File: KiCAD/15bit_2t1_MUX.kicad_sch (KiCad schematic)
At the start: 4 parts, among them U48 74HC257, U49 74HC257, U50 74HC257, U51 74HC257

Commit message: finished schematics and footprint assignments; need to figure out +5v connection issue
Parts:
- U48, U49, U50, U51: footprint (none) -> Package_DIP:DIP-16_W7.62mm
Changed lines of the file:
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@@
 			)
 		)
-		(property "Footprint" ""
+		(property "Footprint" "Package_DIP:DIP-16_W7.62mm"
 			(at 203.2 64.77 0)
 			(effects
@@
 			)
 		)
-		(property "Footprint" ""
+		(property "Footprint" "Package_DIP:DIP-16_W7.62mm"
 			(at 119.38 64.77 0)
 			(effects
@@
 			)
 		)
-		(property "Footprint" ""
+		(property "Footprint" "Package_DIP:DIP-16_W7.62mm"
 			(at 78.74 64.77 0)
 			(effects
@@
 			)
 		)
-		(property "Footprint" ""
+		(property "Footprint" "Package_DIP:DIP-16_W7.62mm"
 			(at 161.29 64.77 0)
 			(effects

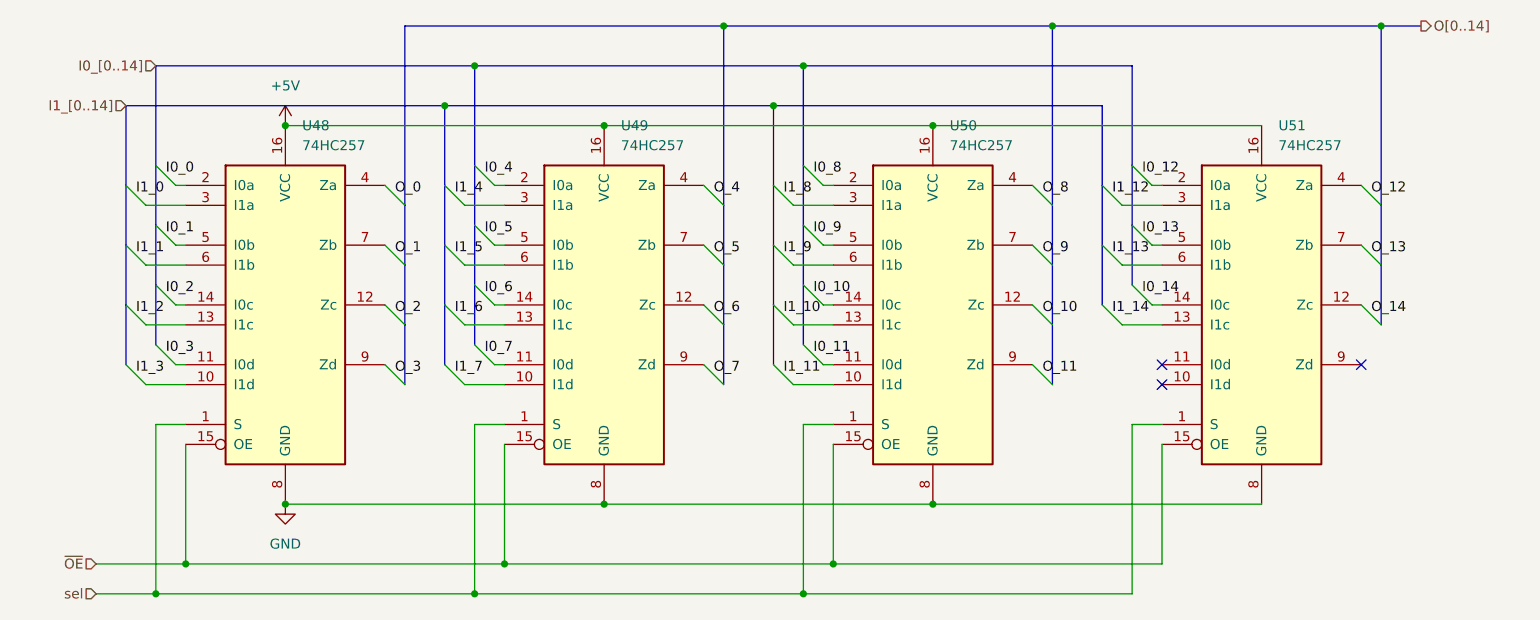
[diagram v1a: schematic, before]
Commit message: fix multiple ERCs that made RAM addrs not connecting
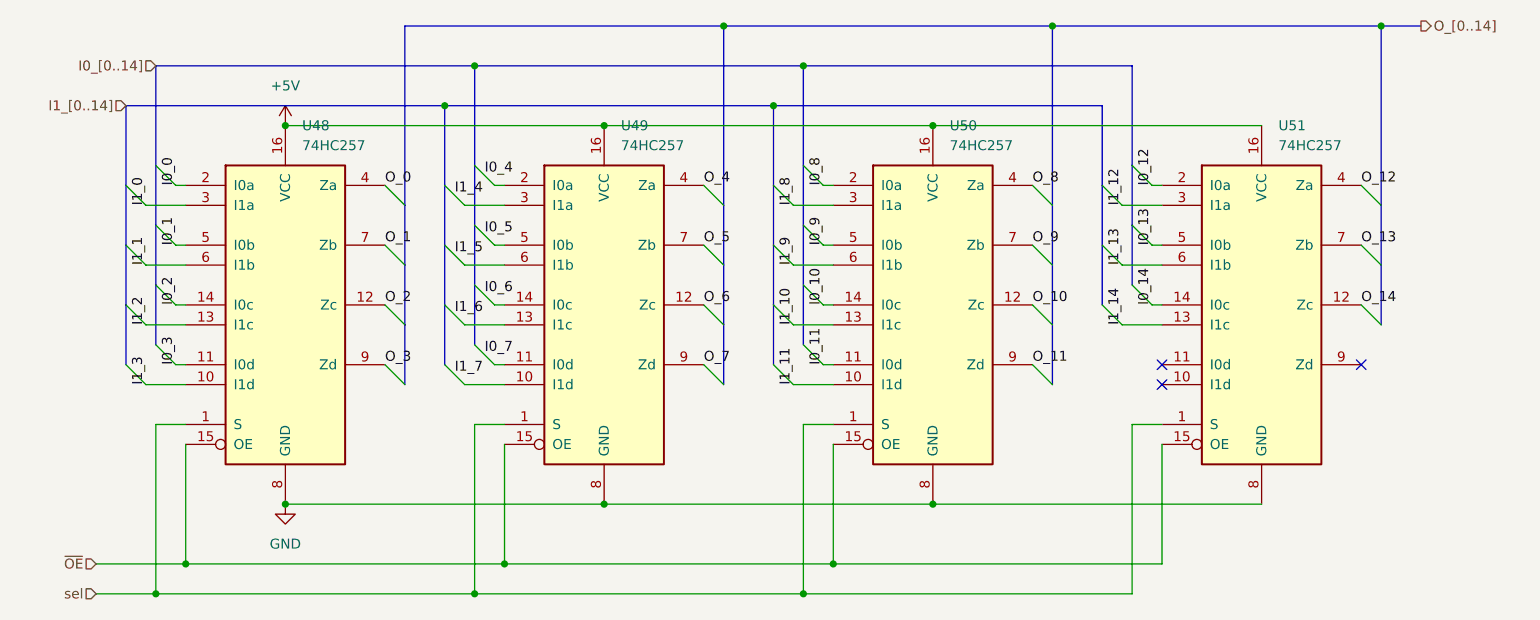
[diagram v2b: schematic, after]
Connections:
- net I0_0: now also U48.2 (I0a)
- net I0_1: now also U48.5 (I0b)
- net I0_10: now also U50.14 (I0c)
- net I0_11: now also U50.11 (I0d)
- net I0_12: now also U51.2 (I0a)
- net I0_13: now also U51.5 (I0b)
- net I0_14: now also U51.14 (I0c)
- net I0_2: now also U48.14 (I0c)
- net I0_3: now also U48.11 (I0d)
- net I0_8: now also U50.2 (I0a)
- net I0_9: now also U50.5 (I0b)
- net I1_0: now also U48.3 (I1a)
- net I1_1: now also U48.6 (I1b)
- net I1_10: now also U50.13 (I1c)
- net I1_11: now also U50.10 (I1d)
- net I1_12: now also U51.3 (I1a)
- net I1_13: now also U51.6 (I1b)
- net I1_14: now also U51.13 (I1c)
- net I1_2: now also U48.13 (I1c)
- net I1_3: now also U48.10 (I1d)
- net I1_8: now also U50.3 (I1a)
- net I1_9: now also U50.6 (I1b)
- net O_0: now also U48.4 (Za)
- net O_1: now also U48.7 (Zb)
- net O_10: now also U50.12 (Zc)
- net O_11: now also U50.9 (Zd)
- net O_12: now also U51.4 (Za)
- net O_13: now also U51.7 (Zb)
- net O_14: now also U51.12 (Zc)
- net O_2: now also U48.12 (Zc)
- net O_3: now also U48.9 (Zd)
- net O_4: now also U49.4 (Za)
- net O_5: now also U49.7 (Zb)
- net O_6: now also U49.12 (Zc)
- net O_7: now also U49.9 (Zd)
- net O_8: now also U50.4 (Za)
- net O_9: now also U50.7 (Zb)
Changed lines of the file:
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@@
 	)
 	(label "I1_9"
-		(at 142.24 58.42 0)
+		(at 143.51 59.69 90)
 		(effects
 			(font
@@
 	)
 	(label "O_7"
-		(at 133.35 73.66 0)
+		(at 132.08 72.39 0)
 		(effects
 			(font
@@
 	)
 	(label "I1_14"
-		(at 184.15 66.04 0)
+		(at 185.42 67.31 90)
 		(effects
 			(font
@@
 	)
 	(label "O_8"
-		(at 175.26 50.8 0)
+		(at 173.99 49.53 0)
 		(effects
 			(font
@@
 	)
 	(label "I0_10"
-		(at 146.05 63.5 0)
+		(at 147.32 64.77 90)
 		(effects
 			(font
@@
 	)
 	(label "O_11"
-		(at 175.26 73.66 0)
+		(at 173.99 72.39 0)
 		(effects
 			(font
@@
 	)
 	(label "O_0"
-		(at 92.71 50.8 0)
+		(at 91.44 49.53 0)
 		(effects
 			(font
@@
 	)
 	(label "I1_3"
-		(at 59.69 73.66 0)
+		(at 60.96 74.93 90)
 		(effects
 			(font
@@
 	)
 	(label "O_10"
-		(at 175.26 66.04 0)
+		(at 173.99 64.77 0)
 		(effects
 			(font
@@
 	)
 	(label "I0_12"
-		(at 187.96 48.26 0)
+		(at 189.23 49.53 90)
 		(effects
 			(font
@@
 	)
 	(label "O_5"
-		(at 133.35 58.42 0)
+		(at 132.08 57.15 0)
 		(effects
 			(font
@@
 	)
 	(label "I1_8"
-		(at 142.24 50.8 0)
+		(at 143.51 52.07 90)
 		(effects
 			(font
@@
 	)
 	(label "O_14"
-		(at 217.17 66.04 0)
+		(at 215.9 64.77 0)
 		(effects
 			(font
@@
 	)
 	(label "O_2"
-		(at 92.71 66.04 0)
+		(at 91.44 64.77 0)
 		(effects
 			(font
@@
 	)
 	(label "O_6"
-		(at 133.35 66.04 0)
+		(at 132.08 64.77 0)
 		(effects
 			(font
@@
 	)
 	(label "I0_0"
-		(at 63.5 48.26 0)
+		(at 64.77 49.53 90)
 		(effects
 			(font
@@
 	)
 	(label "O_12"
-		(at 217.17 50.8 0)
+		(at 215.9 49.53 0)
 		(effects
 			(font
@@
 	)
 	(label "O_1"
-		(at 92.71 58.42 0)
+		(at 91.44 57.15 0)
 		(effects
 			(font
@@
 	)
 	(label "I1_1"
-		(at 59.69 58.42 0)
+		(at 60.96 59.69 90)
 		(effects
 			(font
@@
 	)
 	(label "O_13"
-		(at 217.17 58.42 0)
+		(at 215.9 57.15 0)
 		(effects
 			(font
@@
 	)
 	(label "I0_14"
-		(at 187.96 63.5 0)
+		(at 189.23 64.77 90)
 		(effects
 			(font
@@
 	)
 	(label "I1_10"
-		(at 142.24 66.04 0)
+		(at 143.51 67.31 90)
 		(effects
 			(font
@@
 	)
 	(label "I1_0"
-		(at 59.69 50.8 0)
+		(at 60.96 52.07 90)
 		(effects
 			(font
@@
 	)
 	(label "I1_11"
-		(at 142.24 73.66 0)
+		(at 143.51 74.93 90)
 		(effects
 			(font
@@
 	)
 	(label "I0_2"
-		(at 63.5 63.5 0)
+		(at 64.77 64.77 90)
 		(effects
 			(font
@@
 	)
 	(label "O_9"
-		(at 175.26 58.42 0)
+		(at 173.99 57.15 0)
 		(effects
 			(font
@@
 	)
 	(label "I0_9"
-		(at 146.05 55.88 0)
+		(at 147.32 57.15 90)
 		(effects
 			(font
@@
 	)
 	(label "I1_2"
-		(at 59.69 66.04 0)
+		(at 60.96 67.31 90)
 		(effects
 			(font
@@
 	)
 	(label "O_4"
-		(at 133.35 50.8 0)
+		(at 132.08 49.53 0)
 		(effects
 			(font
@@
 	)
 	(label "O_3"
-		(at 92.71 73.66 0)
+		(at 91.44 72.39 0)
 		(effects
 			(font
@@
 	)
 	(label "I0_3"
-		(at 63.5 71.12 0)
+		(at 64.77 72.39 90)
 		(effects
 			(font
@@
 	)
 	(label "I1_12"
-		(at 184.15 50.8 0)
+		(at 185.42 52.07 90)
 		(effects
 			(font
@@
 	)
 	(label "I0_1"
-		(at 63.5 55.88 0)
+		(at 64.77 57.15 90)
 		(effects
 			(font
@@
 	)
 	(label "I0_13"
-		(at 187.96 55.88 0)
+		(at 189.23 57.15 90)
 		(effects
 			(font
@@
 	)
 	(label "I0_8"
-		(at 146.05 48.26 0)
+		(at 147.32 49.53 90)
 		(effects
 			(font
@@
 	)
 	(label "I1_13"
-		(at 184.15 58.42 0)
+		(at 185.42 59.69 90)
 		(effects
 			(font
@@
 	)
 	(label "I0_11"
-		(at 146.05 71.12 0)
+		(at 147.32 72.39 90)
 		(effects
 			(font
@@
 		)
 	)
-	(hierarchical_label "O[0..14]"
+	(hierarchical_label "O_[0..14]"
 		(shape output)
 		(at 223.52 29.21 0)

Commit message: resolve ERCs for addr combiner
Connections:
- net I0_4: now also U49.2 (I0a)
- net I0_5: now also U49.5 (I0b)
- net I0_6: now also U49.14 (I0c)
- net I0_7: now also U49.11 (I0d)
- net I1_4: now also U49.3 (I1a)
- net I1_5: now also U49.6 (I1b)
- net I1_6: now also U49.13 (I1c)
- net I1_7: now also U49.10 (I1d)
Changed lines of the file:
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@@
 	)
 	(label "I1_7"
-		(at 100.33 73.66 0)
+		(at 101.6 74.93 90)
 		(effects
 			(font
@@
 	)
 	(label "I0_4"
-		(at 104.14 48.26 0)
+		(at 105.41 49.53 90)
 		(effects
 			(font
@@
 	)
 	(label "I0_6"
-		(at 104.14 63.5 0)
+		(at 105.41 64.77 90)
 		(effects
 			(font
@@
 	)
 	(label "I0_7"
-		(at 104.14 71.12 0)
+		(at 105.41 72.39 90)
 		(effects
 			(font
@@
 	)
 	(label "I1_5"
-		(at 100.33 58.42 0)
+		(at 101.6 59.69 90)
 		(effects
 			(font
@@
 	)
 	(label "I1_4"
-		(at 100.33 50.8 0)
+		(at 101.6 52.07 90)
 		(effects
 			(font
@@
 	)
 	(label "I1_6"
-		(at 100.33 66.04 0)
+		(at 101.6 67.31 90)
 		(effects
 			(font
@@
 	)
 	(label "I0_5"
-		(at 104.14 55.88 0)
-		(effects
-			(font
+		(at 105.41 57.15 90)
+		(effects
+			(font
